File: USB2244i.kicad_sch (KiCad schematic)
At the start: 17 parts, among them U17 USB2244I-AEZG-06-TR, X5 24MHz

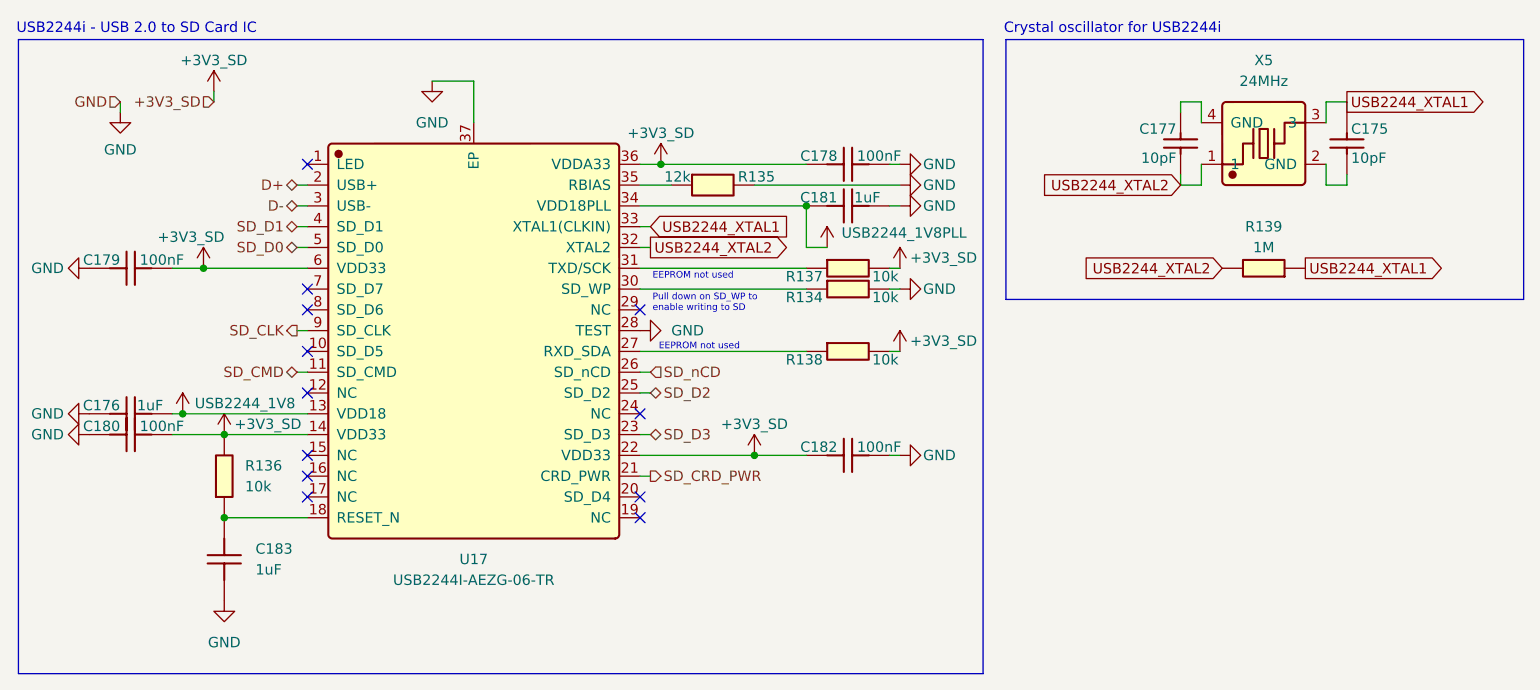
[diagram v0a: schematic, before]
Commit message: Basic Function Review/Documentation of USB2244i
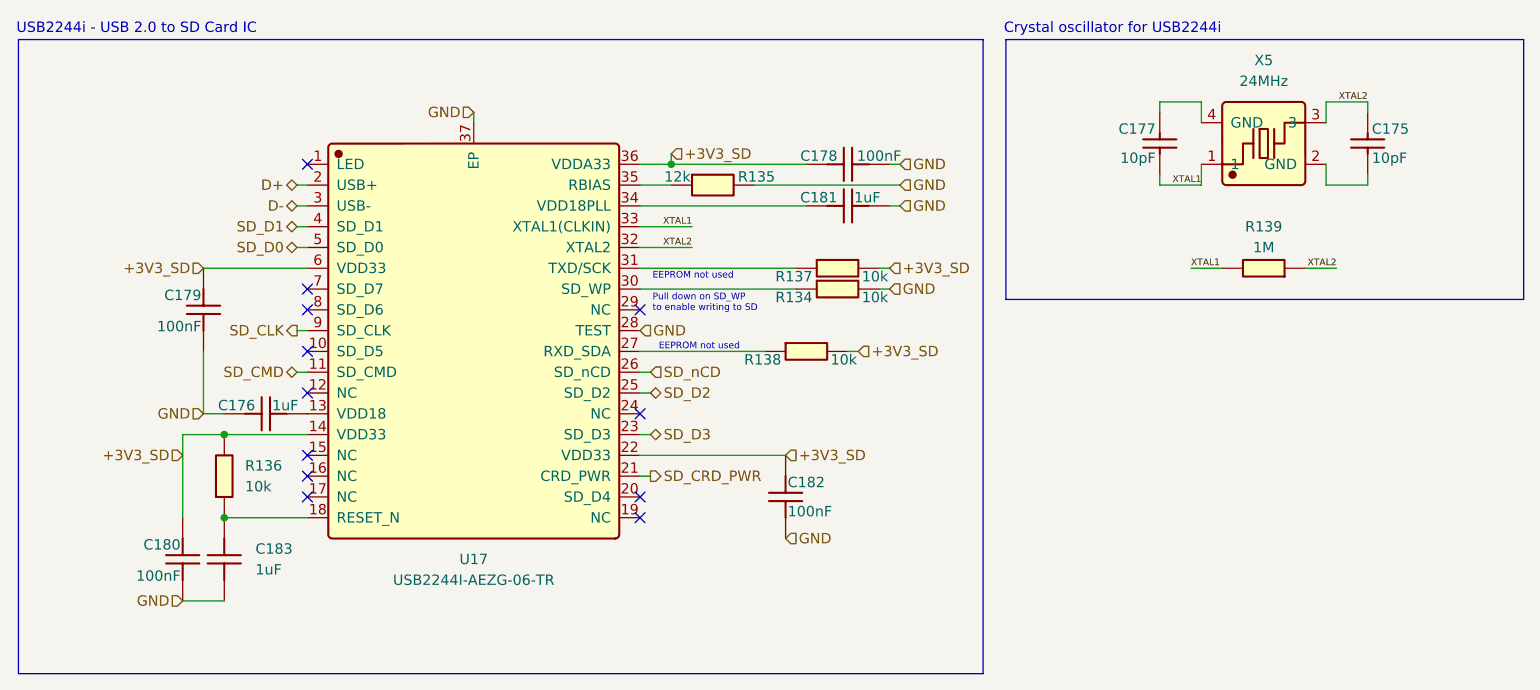
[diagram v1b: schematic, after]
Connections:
- net USB2244_1V8: no longer names the net of C176.1, U17.13 (VDD18)
- net USB2244_1V8PLL: no longer names the net of C181.2, U17.34 (VDD18PLL)
- net USB2244_XTAL1 renamed XTAL2
- net XTAL2: now also U17.32 (XTAL2); no longer U17.33 (XTAL1(CLKIN))
- net USB2244_XTAL2 renamed XTAL1
- net XTAL1: now also U17.33 (XTAL1(CLKIN)); no longer U17.32 (XTAL2)
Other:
- moved on the sheet: C175, C176, C177, C179, R134, R137, R138
